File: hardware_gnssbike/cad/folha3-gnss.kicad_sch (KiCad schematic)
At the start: 13 parts, among them J302 Hirose U.FL-R-SMT-1, U301 u-blox MAX-F10S, U302 TI TXU0204BQAR

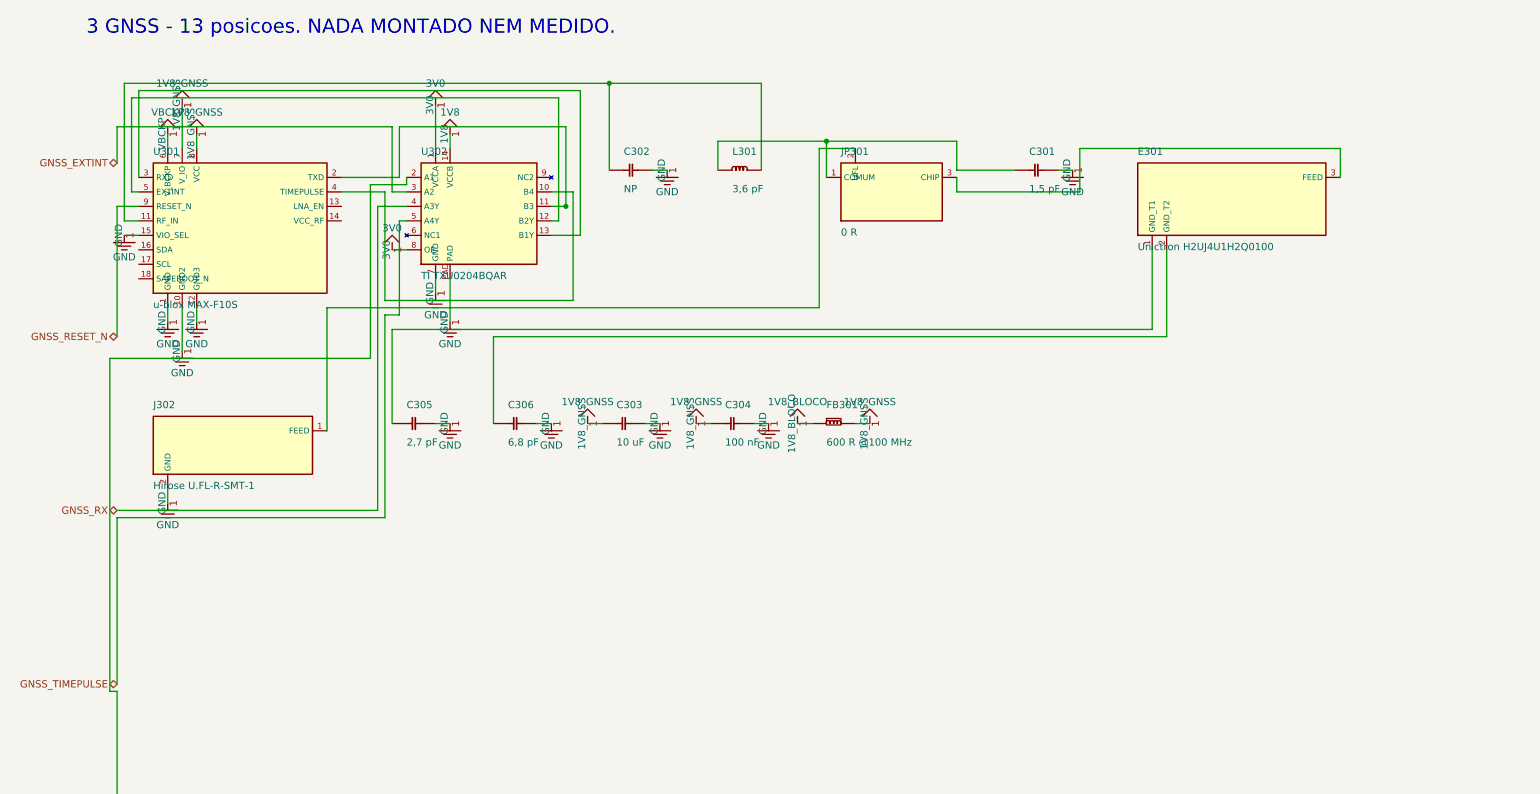
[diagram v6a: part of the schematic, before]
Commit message: feat(hardware): real symbols and real 3D models, from KiCad's own libraries
Two of the owner's asks in one commit, because they turned out to be the
same idea: stop drawing what already exists, reviewed, in the library.

THE SCHEMATIC. 36 of the parts were rectangles with pins around them - the
ICs, the connectors and the display - and a rectangle says nothing. Anyone
reading a schematic recognises a coaxial connector by the circle with the
dot, a switch by the contact that opens, a MOSFET by the channel and the
arrow.

ksym.py reads a symbol out of KiCad's own library - 21.110 of them, every
one reviewed against the KLC - and embeds it in our schematic with our
properties. simbolos.py says which part uses which. Eleven are in, and
ksym.checar() verifies every one pin number by pin number, because a
pretty symbol with the wire on the wrong pin is worse than a correct
rectangle. RF_GPS:MAX-M10S is literally our receiver: 18 pins, 18 names,
the same LCC-18.

Three symbols verify clean and still break the drawing, and they are
parked with the reason MEASURED rather than "did not work": the ADP5091
puts MPPT on the bottom edge beside its three ground pins and the ground
power symbol lands on the MPPT wire; the USB-C stacks four contacts per
point with 5,08 mm stubs and VBUS meets CC1; the ten pins of the display
FPC are all on one edge and two wires cannot reach. Each needs work
somewhere else - the power symbol placer, the placement - not a different
symbol.

Three bugs were found and fixed on the way, all in the router, all of the
same family: it assumed things about symbols that are only true of the
ones this project draws.

  - Symbols from KiCad are NOT centred on their origin. A
    Conn_01x10_Socket has its drawing at x -1,27 to 0 and all ten pins at
    x = -5,08. Treated as centred, pins fall inside the obstacle, the
    router cannot reach them from outside and goes over them instead -
    and two nets that touch are one net, with nothing in the drawing
    sa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
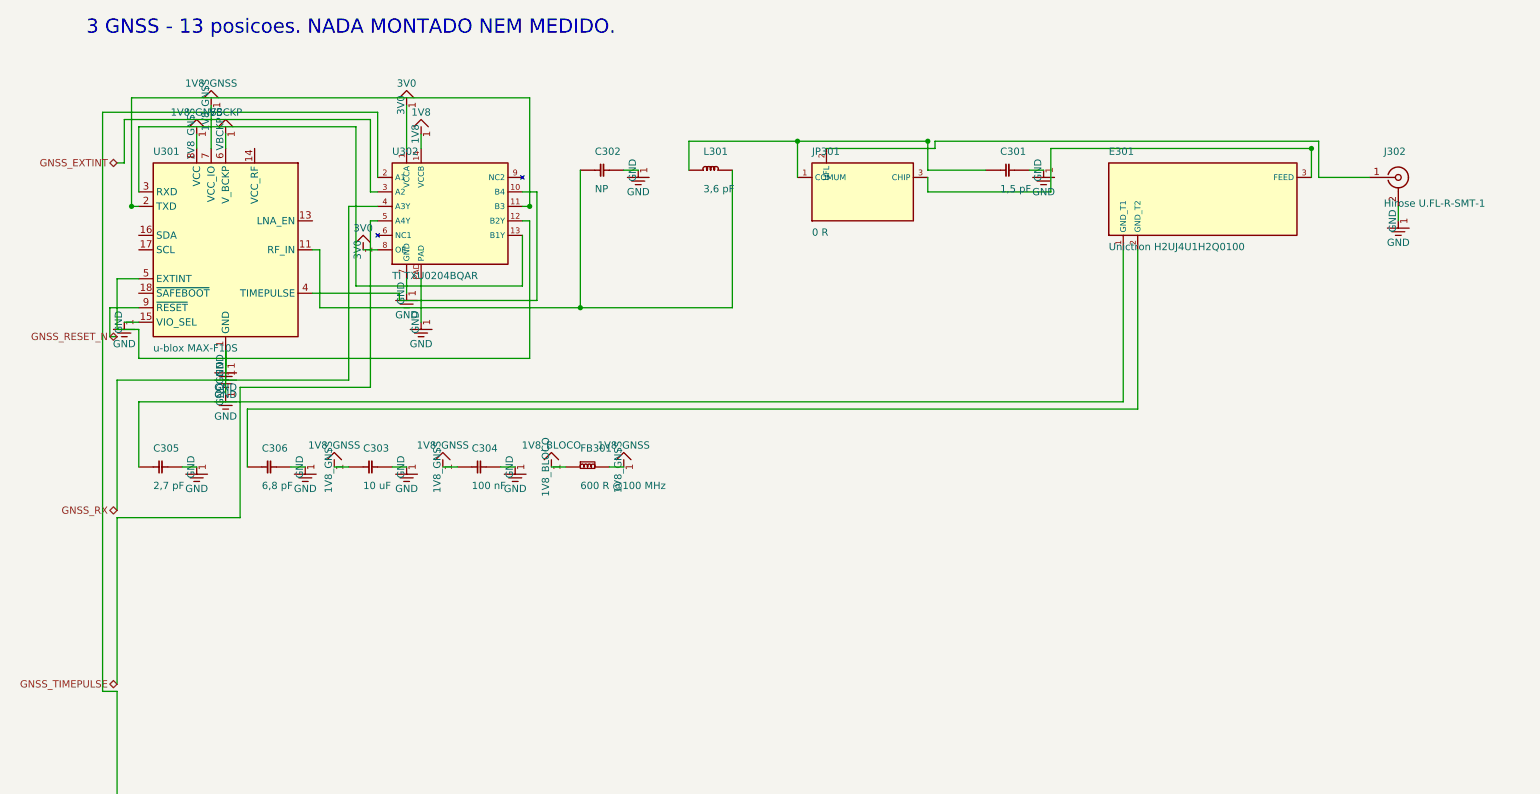
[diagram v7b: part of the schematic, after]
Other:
- moved on the sheet: C301, C302, C303, C304, C305, C306, E301, FB301, JP301, L301, U302

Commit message: fix(hardware): the debug connector had RESET on the wrong contact
This one would have cost a board. The Tag-Connect TC2030 footprint had
pin 3 as no-connect and RESET on pin 6. The manufacturer's own data
sheet, TC2030-CTX_1.pdf, table "Connections", says the opposite: on the
six-pin footprint it is 3 = nRESET and 6 = SWO/TDO.

Where the mistake came from is worth writing down, because it is easy to
make twice: 1 VCC, 2 SWDIO, 3 GND, 4 SWCLK, 5 GND, 6 SWO is the
numbering of the ten-way Cortex header on the PROBE side, not of the
six-pin footprint on the board. Mixing the two gives exactly what was
written here.

What it would have done: the probe's nRESET is an open drain output, so
it would have driven nothing, and the MCU's reset would have hung off
the probe's SWO INPUT. Nothing burns - SWO runs target to probe, there
is no short - but the debugger can never reset the target: no connect
under reset, no pin reset. On an nRF54LM20A that reboots from task_wdt
or reconfigures its SWD pins, that removes the standard way out and
leaves only a full CTRL-AP erase.

The documentation carried a worse version still. 06 had GND on contact 3,
which fabricated would tie the probe's open-drain nRESET to copper
ground and hold the target in reset forever.

The project's own notes had predicted this exact variant - 06 carried a
CAUTION saying so and README an open checklist item. It was that one, and
it was caught before layout. Both are now closed, and the connector's
pin 6 is recorded as SWO with what is still unknown about it: which pad
of the ME54BS13 exposes SWO, which would give printf over ITM during
bring-up.

Fixed in parts.py, nets.py, 03-netlist.md, 06-conectores-e-pontos-de-teste.md,
07-sequencias-e-protecao.md and README.md.

Verified: check_sch and check_pcb pass, 78 of 78 diagrams render, 1529
links and none broken.
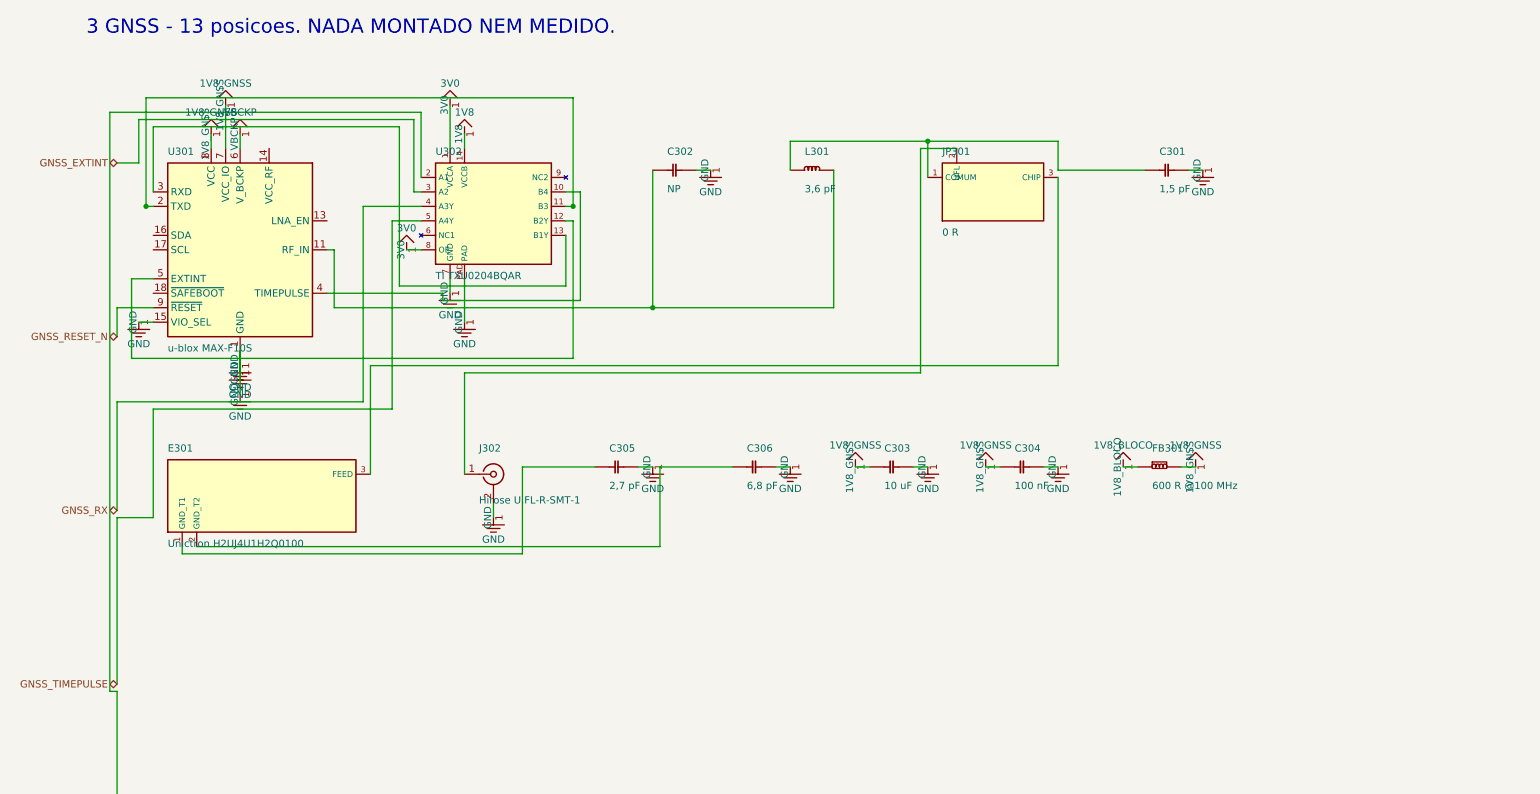
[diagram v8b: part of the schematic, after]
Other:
- moved on the sheet: C301, C302, C303, C304, C305, C306, E301, FB301, J302, JP301, L301, U301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
